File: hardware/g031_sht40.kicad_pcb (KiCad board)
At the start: 2 copper layers, 75 x 47 mm, 30 parts, among them J1 Screw_Terminal_01x02, J2 Conn_01x06_Pin, J3 Conn_01x02_Pin, J4 Screw_Terminal_01x02, J5 Conn_01x03_Pin, J6 Conn_01x04_Pin, J7 Conn_01x04_Pin, J8 Conn_01x08_Pin, SW1 SW_Push, U1 AEM10941 module, U2 SHT40 module, U3 STM32G031F6Px, U4 E-Ink display module

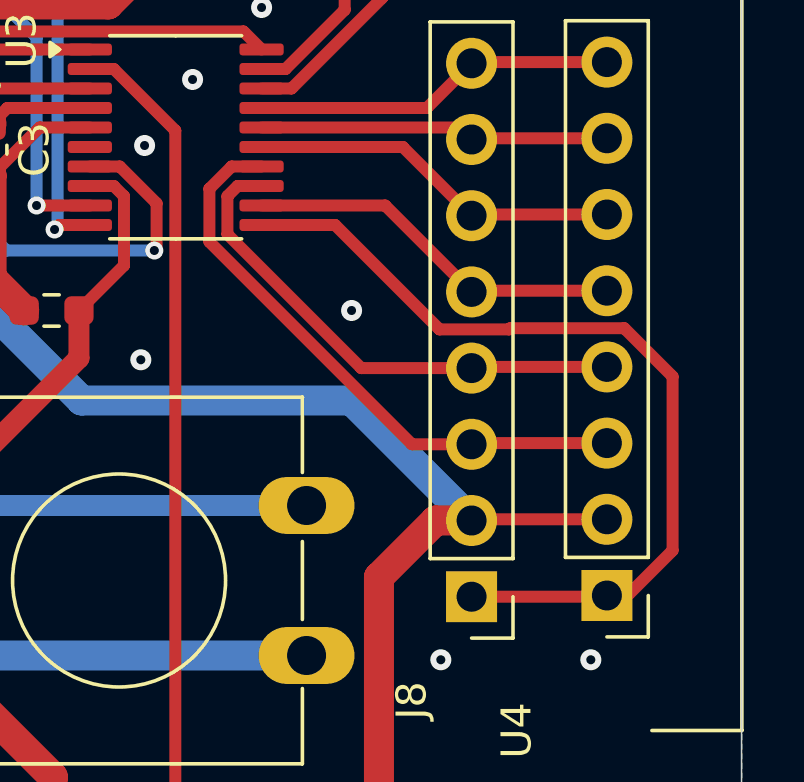
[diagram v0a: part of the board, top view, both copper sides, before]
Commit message: Fix pin assignments for EPD control
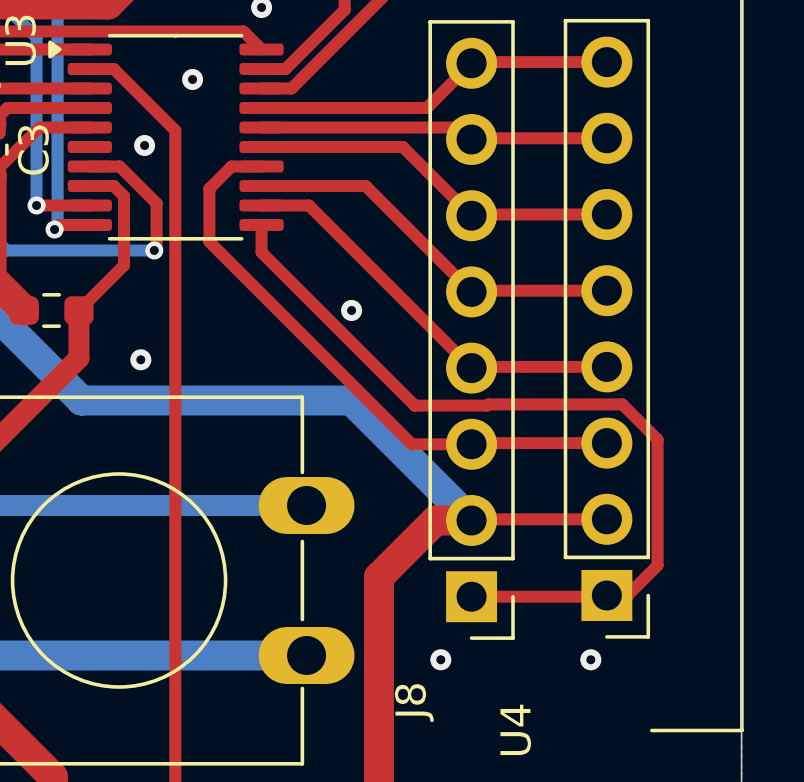
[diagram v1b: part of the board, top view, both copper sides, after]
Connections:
- U3 pad 12: Net-(J8-Pin_5) -> Net-(J8-Pin_4)
- U3 pad 13: Net-(J8-Pin_4) -> Net-(J8-Pin_5)
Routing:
- net Net-(J8-Pin_4): track 17.1 -> 13.8 mm
- net /EPD_VCC: track 29.0 -> 27.6 mm
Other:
- board text added: "G031_SHT40 rev 0.2"
- board text removed: "G031_SHT40 rev 0.1"
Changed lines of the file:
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@@
 	(title_block
 		(title "G031_SHT40")
-		(date "2026-05-17")
-		(rev "0.1")
+		(date "2026-06-08")
+		(rev "0.2")
 		(company "Iurii Volkov")
 	)
@@
 			(layers "F.Cu" "F.Mask" "F.Paste")
 			(roundrect_rratio 0.25)
-			(net 26 "Net-(J8-Pin_5)")
+			(net 14 "Net-(J8-Pin_4)")
 			(pinfunction "PA5")
 			(pintype "bidirectional")
@@
 			(layers "F.Cu" "F.Mask" "F.Paste")
 			(roundrect_rratio 0.25)
-			(net 14 "Net-(J8-Pin_4)")
+			(net 26 "Net-(J8-Pin_5)")
 			(pinfunction "PA6")
 			(pintype "bidirectional")
@@
 		)
 	)
-	(gr_text "G031_SHT40 rev 0.1"
+	(gr_text "G031_SHT40 rev 0.2"
 		(at 121 65 90)
 		(layer "B.SilkS")
@@
 	)
 	(segment
-		(start 166 77.92)
-		(end 162.321208 77.92)
-		(width 0.4)
-		(layer "F.Cu")
-		(net 14)
-	)
-	(segment
 		(start 170.51 77.88)
 		(end 166.04 77.88)
@@
 	)
 	(segment
-		(start 157.8615 72.189708)
-		(end 158.201208 71.85)
-		(width 0.4)
-		(layer "F.Cu")
-		(net 14)
-	)
-	(segment
-		(start 162.321208 77.92)
-		(end 157.8615 73.460292)
+		(start 166 77.92)
+		(end 160.58 72.5)
 		(width 0.4)
 		(layer "F.Cu")
@@
 	)
 	(segment
-		(start 157.8615 73.460292)
-		(end 157.8615 72.189708)
-		(width 0.4)
-		(layer "F.Cu")
-		(net 14)
-	)
-	(segment
-		(start 158.201208 71.85)
-		(end 159 71.85)
+		(start 160.58 72.5)
+		(end 159 72.5)
 		(width 0.4)
 		(layer "F.Cu")
@@
 	)
 	(segment
-		(start 172.7 78.2)
-		(end 171.091 76.591)
+		(start 170.51 85.5)
+		(end 171.2 85.5)
 		(width 0.4)
 		(layer "F.Cu")
@@
 	)
 	(segment
-		(start 167.291 76.591)
-		(end 167.251 76.631)
+		(start 166.518182 79.171)
+		(end 164.108925 79.171)
 		(width 0.4)
 		(layer "F.Cu")
@@
 	)
 	(segment
-		(start 172.7 84)
-		(end 172.7 78.2)
+		(start 172.2 80.302818)
+		(end 171.028182 79.131)
 		(width 0.4)
 		(layer "F.Cu")
@@
 	)
 	(segment
-		(start 161.45 73.15)
-		(end 159 73.15)
+		(start 171.028182 79.131)
+		(end 166.558182 79.131)
 		(width 0.4)
 		(layer "F.Cu")
@@
 	)
 	(segment
-		(start 170.51 85.5)
-		(end 171.2 85.5)
+		(start 166.558182 79.131)
+		(end 166.518182 79.171)
 		(width 0.4)
 		(layer "F.Cu")
@@
 	(segment
 		(start 171.2 85.5)
-		(end 172.7 84)
+		(end 172.2 84.5)
 		(width 0.4)
 		(layer "F.Cu")
@@
 	)
 	(segment
-		(start 164.931 76.631)
-		(end 161.45 73.15)
+		(start 159 74.062075)
+		(end 159 73.15)
 		(width 0.4)
 		(layer "F.Cu")
@@
 	)
 	(segment
-		(start 167.251 76.631)
-		(end 164.931 76.631)
+		(start 172.2 84.5)
+		(end 172.2 80.302818)
 		(width 0.4)
 		(layer "F.Cu")
@@
 	)
 	(segment
-		(start 171.091 76.591)
-		(end 167.291 76.591)
+		(start 164.108925 79.171)
+		(end 159 74.062075)
 		(width 0.4)
 		(layer "F.Cu")
@@
 	)
 	(segment
-		(start 166 75.38)
-		(end 163.12 72.5)
+		(start 166.04 75.34)
+		(end 166 75.38)
 		(width 0.4)
 		(layer "F.Cu")
@@
 	)
 	(segment
-		(start 166.04 75.34)
-		(end 166 75.38)
+		(start 166 75.38)
+		(end 162.47 71.85)
 		(width 0.4)
 		(layer "F.Cu")
@@
 	)
 	(segment
-		(start 170.51 75.34)
-		(end 166.04 75.34)
+		(start 162.47 71.85)
+		(end 159 71.85)
 		(width 0.4)
 		(layer "F.Cu")
@@
 	)
 	(segment
-		(start 163.12 72.5)
-		(end 159 72.5)
+		(start 170.51 75.34)
+		(end 166.04 75.34)
 		(width 0.4)
 		(layer "F.Cu")
